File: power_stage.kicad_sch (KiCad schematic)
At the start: 15 parts, among them SW4 SW_SPDT, U6 TPS63001, U9 TPS63002

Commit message: some updates
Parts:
- C10, C13, C15, C16, C17, C2: footprint (none) -> Capacitor_SMD:C_0603_1608Metric
- C18, C9: footprint (none) -> Capacitor_SMD:C_0402_1005Metric
- R4, R5: footprint (none) -> Resistor_SMD:R_0402_1005Metric
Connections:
- net at C18.1, R5.2, U9.8 (VINA): now also U9.7 (PS/SYNC)
- net at C9.1, R4.2, U6.8 (VINA): now also U6.7 (PS/SYNC)
- net +3.3V renamed +3V3
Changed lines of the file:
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@@
+	)
+	(junction
+		(at 129.54 57.15)
+		(diameter 0)
+		(color 0 0 0 0)
 	)
 	(junction
@@
 	)
 	(junction
+		(at 129.54 119.38)
+		(diameter 0)
+		(color 0 0 0 0)
+	)
+	(junction
 		(at 121.92 60.96)
 		(diameter 0)
@@
 	(wire
 		(pts
-			(xy 129.54 114.3) (xy 129.54 123.19)
+			(xy 129.54 114.3) (xy 129.54 119.38)
 		)
 		(stroke
@@
 	(wire
 		(pts
+			(xy 129.54 119.38) (xy 138.43 119.38)
+		)
+		(stroke
+			(width 0)
+			(type default)
+		)
+	)
+	(wire
+		(pts
 			(xy 147.32 138.43) (xy 148.59 138.43)
 		)
@@
 	(wire
 		(pts
-			(xy 130.81 119.38) (xy 138.43 119.38)
-		)
-		(stroke
-			(width 0)
-			(type default)
-		)
-	)
-	(wire
-		(pts
 			(xy 133.35 121.92) (xy 133.35 123.19)
 		)
@@
 	(wire
 		(pts
+			(xy 129.54 57.15) (xy 129.54 60.96)
+		)
+		(stroke
+			(width 0)
+			(type default)
+		)
+	)
+	(wire
+		(pts
+			(xy 129.54 57.15) (xy 138.43 57.15)
+		)
+		(stroke
+			(width 0)
+			(type default)
+		)
+	)
+	(wire
+		(pts
 			(xy 167.64 49.53) (xy 167.64 60.96)
 		)
@@
 	(wire
 		(pts
-			(xy 129.54 52.07) (xy 129.54 60.96)
+			(xy 129.54 52.07) (xy 129.54 57.15)
 		)
 		(stroke
@@
 	(wire
 		(pts
-			(xy 130.81 57.15) (xy 138.43 57.15)
-		)
-		(stroke
-			(width 0)
-			(type default)
-		)
-	)
-	(wire
-		(pts
 			(xy 147.32 138.43) (xy 147.32 139.7)
 		)
@@
 		(pts
 			(xy 138.43 111.76) (xy 121.92 111.76)
+		)
+		(stroke
+			(width 0)
+			(type default)
+		)
+	)
+	(wire
+		(pts
+			(xy 129.54 119.38) (xy 129.54 123.19)
 		)
 		(stroke
@@
 			)
 		)
-		(property "Footprint" ""
+		(property "Footprint" "Capacitor_SMD:C_0603_1608Metric"
 			(at 111.4552 69.85 0)
 			(effects
@@
 			)
 		)
-		(property "Footprint" ""
+		(property "Footprint" "Capacitor_SMD:C_0603_1608Metric"
 			(at 111.4552 132.08 0)
 			(effects
@@
 			)
 		)
-		(property "Footprint" ""
+		(property "Footprint" "Capacitor_SMD:C_0402_1005Metric"
 			(at 122.8852 132.08 0)
 			(effects
@@
 	)
 	(symbol
+		(lib_id "power:+3V3")
+		(at 179.07 46.99 0)
+		(unit 1)
+		(exclude_from_sim no)
+		(in_bom yes)
+		(on_board yes)
+		(dnp no)
+		(fields_autoplaced yes)
+		(property "Reference" "#PWR010"
+			(at 179.07 50.8 0)
+			(effects
+				(font
+					(size 1.27 1.27)
+				)
+				(hide yes)
+			)
+		)
+		(property "Value" "+3V3"
+			(at 179.07 41.91 0)
+			(effects
+				(font
+					(size 1.27 1.27)
+				)
+			)
+		)
+		(property "Footprint" ""
+			(at 179.07 46.99 0)
+			(effects
+				(font
+					(size 1.27 1.27)
+				)
+				(hide yes)
+			)
+		)
+		(property "Datasheet" ""
+			(at 179.07 46.99 0)
+			(effects
+				(font
+					(size 1.27 1.27)
+				)
+				(hide yes)
+			)
+		)
+		(property "Description" "Power symbol creates a global label with name \"+3V3\""
+			(at 179.07 46.99 0)
+			(effects
+				(font
+					(size 1.27 1.27)
+				)
+				(hide yes)
+			)
+		)
+		(pin "1"
+		)
+		(instances
+			(project ""
+				(path "/0461baee-3b25-4e1a-a5c1-d76b4b99c66c/0d6b5693-2a71-4edb-b834-69af52140ea0"
+					(reference "#PWR010")
+					(unit 1)
+				)
+			)
+		)
+	)
+	(symbol
 		(lib_id "Device:R")
 		(at 121.92 118.11 0)
@@
 			)
 		)
-		(property "Footprint" ""
+		(property "Footprint" "Resistor_SMD:R_0402_1005Metric"
 			(at 120.142 118.11 90)
 			(effects
@@
 			)
 		)
-		(property "Footprint" ""
+		(property "Footprint" "Capacitor_SMD:C_0603_1608Metric"
 			(at 180.0352 68.58 0)
 			(effects
@@
 			)
 		)
-		(property "Footprint" ""
+		(property "Footprint" "Capacitor_SMD:C_0603_1608Metric"
 			(at 168.6052 130.81 0)
 			(effects
@@
 			)
 		)
-		(property "Footprint" ""
+		(property "Footprint" "Capacitor_SMD:C_0603_1608Metric"
 			(at 168.6052 68.58 0)
 			(effects
@@
 	)
 	(symbol
-		(lib_id "power:+3.3V")
-		(at 179.07 46.99 0)
-		(unit 1)
-		(exclude_from_sim no)
-		(in_bom yes)
-		(on_board yes)
-		(dnp no)
-		(fields_autoplaced yes)
-		(property "Reference" "#PWR062"
-			(at 179.07 50.8 0)
-			(effects
-				(font
-					(size 1.27 1.27)
-				)
-				(hide yes)
-			)
-		)
-		(property "Value" "+3.3V"
-			(at 179.07 41.91 0)
-			(effects
-				(font
-					(size 1.27 1.27)
-				)
-			)
-		)
-		(property "Footprint" ""
-			(at 179.07 46.99 0)
-			(effects
-				(font
-					(size 1.27 1.27)
-				)
-				(hide yes)
-			)
-		)
-		(property "Datasheet" ""
-			(at 179.07 46.99 0)
-			(effects
-				(font
-					(size 1.27 1.27)
-				)
-				(hide yes)
-			)
-		)
-		(property "Description" "Power symbol creates a global label with name \"+3.3V\""
-			(at 179.07 46.99 0)
-			(effects
-				(font
-					(size 1.27 1.27)
-				)
-				(hide yes)
-			)
-		)
-		(pin "1"
-		)
-		(instances
-			(project ""
-				(path "/0461baee-3b25-4e1a-a5c1-d76b4b99c66c/0d6b5693-2a71-4edb-b834-69af52140ea0"
-					(reference "#PWR062")
-					(unit 1)
-				)
-			)
-		)
-	)
-	(symbol
 		(lib_id "Device:C")
 		(at 179.07 127 0)
@@
 			)
 		)
-		(property "Footprint" ""
+		(property "Footprint" "Capacitor_SMD:C_0603_1608Metric"
 			(at 180.0352 130.81 0)
 			(effects
@@
 			)
 		)
-		(property "Footprint" ""
+		(property "Footprint" "Resistor_SMD:R_0402_1005Metric"
 			(at 120.142 55.88 90)
 			(effects
@@
 			)
 		)
-		(property "Footprint" ""
+		(property "Footprint" "Capacitor_SMD:C_0402_1005Metric"
 			(at 122.8852 69.85 0)
 			(effects

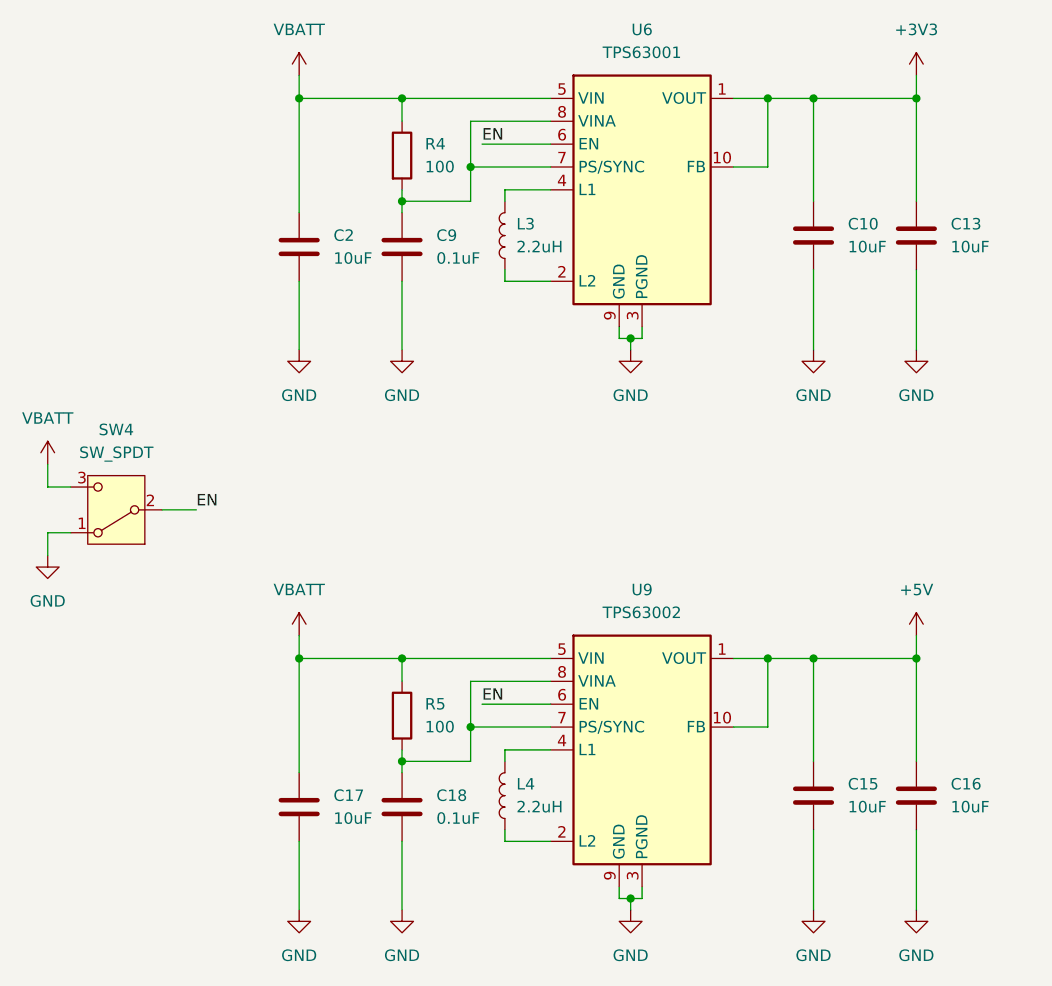
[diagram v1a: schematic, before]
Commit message: complete routing
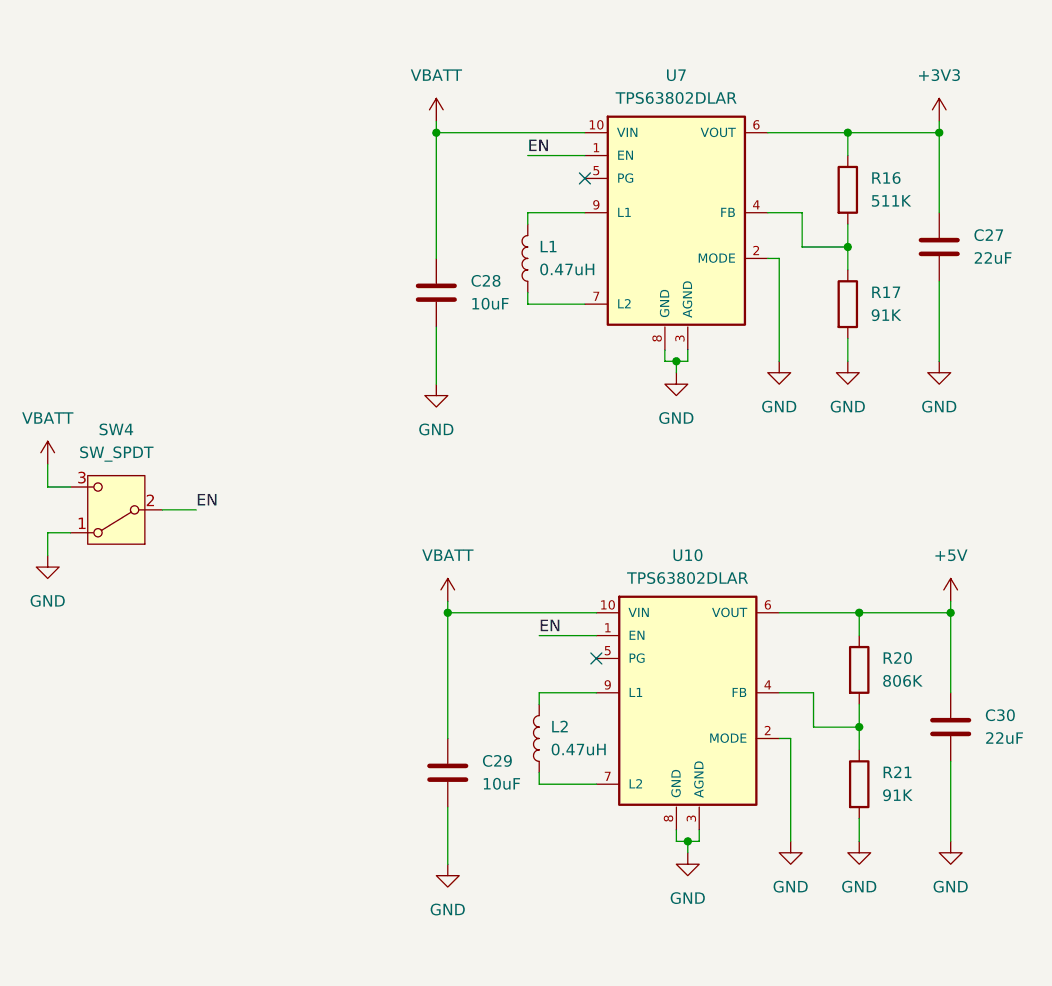
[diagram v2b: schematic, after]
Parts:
- removed C10, C13, C15, C16, C17, C2: 10uF, Capacitor_SMD:C_0603_1608Metric, symbol Device:C
- removed C18, C9: 0.1uF, Capacitor_SMD:C_0402_1005Metric, symbol Device:C
- removed L3, L4: 2.2uH, Inductor_SMD:L_Coilcraft_LPS3010, symbol Device:L
- removed R4, R5: 100, Resistor_SMD:R_0402_1005Metric, symbol Device:R
- removed U6: TPS63001, Package_SON:Texas_DRC0010J_ThermalVias, symbol Regulator_Switching:TPS63001
- removed U9: TPS63002, Package_SON:Texas_DRC0010J_ThermalVias, symbol Regulator_Switching:TPS63002
- added C27, C30: 22uF, Capacitor_SMD:C_0603_1608Metric, symbol Device:C
- added C28, C29: 10uF, Capacitor_SMD:C_0603_1608Metric, symbol Device:C
- added L1, L2: 0.47uH, Inductor_SMD:L_Changjiang_FNR4015S, symbol Device:L
- added R16: 511K, Resistor_SMD:R_0402_1005Metric, symbol Device:R
- added R17, R21: 91K, Resistor_SMD:R_0402_1005Metric, symbol Device:R
- added R20: 806K, Resistor_SMD:R_0402_1005Metric, symbol Device:R
- added U10, U7: TPS63802DLAR, TPS63802DLAR:VREG_TPS63802DLAR, symbol TPS63802DLAR:TPS63802DLAR
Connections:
- net +3V3: now also C27.1, R16.1, U7.6 (VOUT)
- net +5V: now also C30.1, R20.1, U10.6 (VOUT)
- net EN: now also U10.1 (EN), U7.1 (EN)
- net GND: now also C27.2, C28.2, C29.2, C30.2, R17.2, R21.2, U10.2 (MODE), U10.3 (AGND), U10.8 (GND), U7.2 (MODE), U7.3 (AGND), U7.8 (GND)
- net VBATT: now also C28.1, C29.1, U10.10 (VIN), U7.10 (VIN)
- new net: R20.2, R21.1, U10.4 (FB)
- new net: L2.1, U10.7 (L2)
- new net: L2.2, U10.9 (L1)
- new net: L1.1, U7.7 (L2)
- new net: L1.2, U7.9 (L1)
- new net: R16.2, R17.1, U7.4 (FB)
- no-connect marks 0 -> 2
